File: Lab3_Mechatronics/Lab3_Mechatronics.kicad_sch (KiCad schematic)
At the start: 19 parts, among them Q1 Q_Photo_NPN, Q2 NMOS

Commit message: DO NOT USE 220 SHUNT 1K
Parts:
- added C1: 0.1u, symbol Device:C
- R3: value 220 -> 10k
- R7: value 1k -> 47k
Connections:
- net GND: now also C1.2
- net at D1.1 (K), L1.1, V3.1: now also C1.1
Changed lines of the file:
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@@
   (junction (at 66.04 113.03) (diameter 0) (color 0 0 0 0)
+  )
+  (junction (at 36.83 90.17) (diameter 0) (color 0 0 0 0)
+  )
+  (junction (at 36.83 111.76) (diameter 0) (color 0 0 0 0)
   )
   (junction (at 114.3 110.49) (diameter 0) (color 0 0 0 0)
@@
     (stroke (width 0) (type default))
   )
+  (wire (pts (xy 21.59 111.76) (xy 36.83 111.76))
+    (stroke (width 0) (type default))
+  )
   (wire (pts (xy 114.3 110.49) (xy 114.3 119.38))
     (stroke (width 0) (type default))
@@
     (stroke (width 0) (type default))
   )
+  (wire (pts (xy 21.59 90.17) (xy 36.83 90.17))
+    (stroke (width 0) (type default))
+  )
   (wire (pts (xy 54.61 128.27) (xy 54.61 138.43))
     (stroke (width 0) (type default))
   )
   (wire (pts (xy 66.04 113.03) (xy 66.04 115.57))
+    (stroke (width 0) (type default))
+  )
+  (wire (pts (xy 21.59 90.17) (xy 21.59 100.33))
     (stroke (width 0) (type default))
   )
@@
   )
   (wire (pts (xy 35.56 120.65) (xy 43.18 120.65))
+    (stroke (width 0) (type default))
+  )
+  (wire (pts (xy 21.59 107.95) (xy 21.59 111.76))
     (stroke (width 0) (type default))
   )
@@
       (effects (font (size 1.27 1.27)) (justify right))
     )
-    (property "Value" "1k" (at 57.15 125.73 0)
+    (property "Value" "47k" (at 57.15 125.73 0)
       (effects (font (size 1.27 1.27)) (justify right))
     )
@@
       (effects (font (size 1.27 1.27)))
     )
-    (property "Value" "220" (at 46.99 116.84 90)
+    (property "Value" "10k" (at 46.99 116.84 90)
       (effects (font (size 1.27 1.27)))
     )
@@
         )
       )
+    )
+  )
+  (symbol (lib_id "Device:C") (at 21.59 104.14 0) (unit 1)
+    (in_bom yes) (on_board yes) (dnp no) (fields_autoplaced)
+    (property "Reference" "C1" (at 25.4 102.87 0)
+      (effects (font (size 1.27 1.27)) (justify left))
+    )
+    (property "Value" "0.1u" (at 25.4 105.41 0)
+      (effects (font (size 1.27 1.27)) (justify left))
+    )
+    (property "Footprint" "" (at 22.5552 107.95 0)
+      (effects (font (size 1.27 1.27)) hide)
+    )
+    (property "Datasheet" "~" (at 21.59 104.14 0)
+      (effects (font (size 1.27 1.27)) hide)
+    )
+    (pin "1")
+    (pin "2")
+    (instances
+      (project "Lab3_Mechatronics"
+        (path "/33824bd4-7a24-4c2c-90db-ac51522648a8"
+          (reference "C1") (unit 1)
+        )
+      )

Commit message: replaced 220 with 470 ohm resistor
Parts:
- R1: value 220 -> 470
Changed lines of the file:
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@@
       (effects (font (size 1.27 1.27)) (justify left))
     )
-    (property "Value" "220" (at 46.99 43.18 0)
+    (property "Value" "470" (at 46.99 43.18 0)
       (effects (font (size 1.27 1.27)) (justify left))
     )

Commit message: replaced collector resistor with 47kohm
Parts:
- R2: value 4.7k -> 47k
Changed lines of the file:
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@@
       (effects (font (size 1.27 1.27)) (justify left))
     )
-    (property "Value" "4.7k" (at 90.17 43.18 0)
+    (property "Value" "47k" (at 90.17 43.18 0)
       (effects (font (size 1.27 1.27)) (justify left))
     )

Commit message: changed voltage source, and comment on back emf
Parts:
- V3: value 9 -> 10
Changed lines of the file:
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@@
     (fill (type none))
   )
-  (text_box "Note: Your backemf voltage here will not be negative, instead it will appear as being above the 12V voltage source"
+  (text_box "Note: Your backemf voltage on the oscilloscope will not be negative, instead it will appear as a voltage above the 10V voltage source."
     (at 72.39 82.55 0) (size 36.83 10.16)
     (stroke (width 0) (type default))
@@
       (effects (font (size 1.27 1.27) (color 0 0 1 1)) (justify left))
     )
-    (property "Value" "9" (at 31.75 104.14 0)
+    (property "Value" "10" (at 31.75 104.14 0)
       (effects (font (size 1.27 1.27) (color 0 0 1 1)) (justify left))
     )

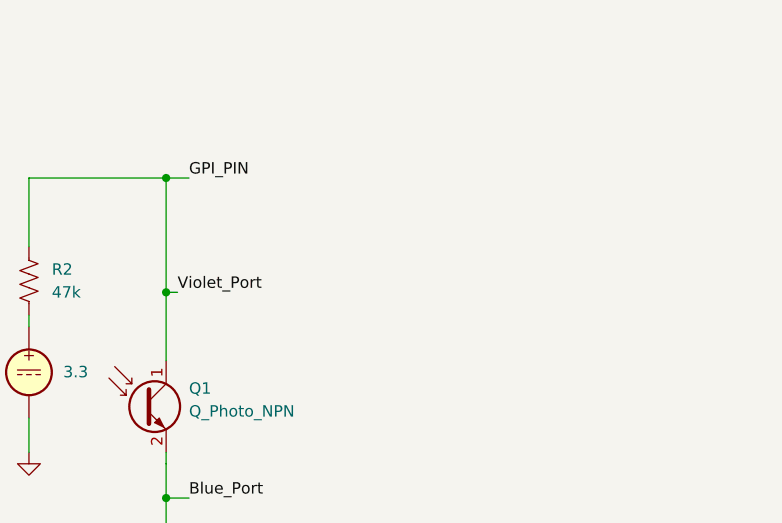
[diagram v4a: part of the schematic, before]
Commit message: added schmitt trigger to this circuit
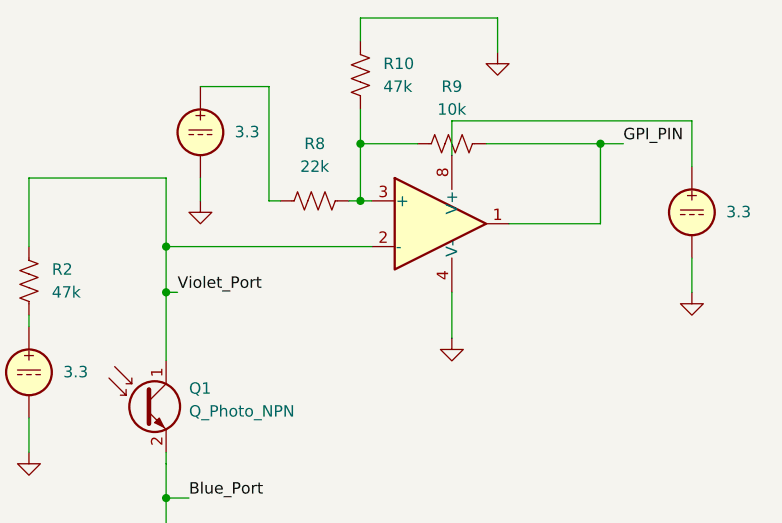
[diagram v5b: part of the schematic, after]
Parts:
- added R10: 47k, symbol Device:R_US
- added R8: 22k, symbol Device:R_US
- added R9: 10k, symbol Device:R_US
- added U1: LM358, symbol Amplifier_Operational:LM358
- added V5, V6: 3.3, symbol Simulation_SPICE:VDC
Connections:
- net GND: now also R10.2, U1.4 (V-), V5.2, V6.2
- net GPI_PIN: now also R9.2, U1.1; no longer Q1.1 (C), R2.1
- new net: U1.8 (V+), V5.1
- new net: R10.1, R8.2, R9.1, U1.3 (+)
- new net: R8.1, V6.1
- new net Violet_Port: Q1.1 (C), R2.1, U1.2 (-)

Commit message: unfinished lab 4 schem(in progress)
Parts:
- added C2: 0.1u, symbol Device:C
- R10: value 47k -> 22k
- R9: value 10k -> 47k
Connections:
- net GND: now also R9.2, C2.2; no longer R10.2
- net GPI_PIN: now also R10.2; no longer R9.2
- net Violet_Port: now also C2.1

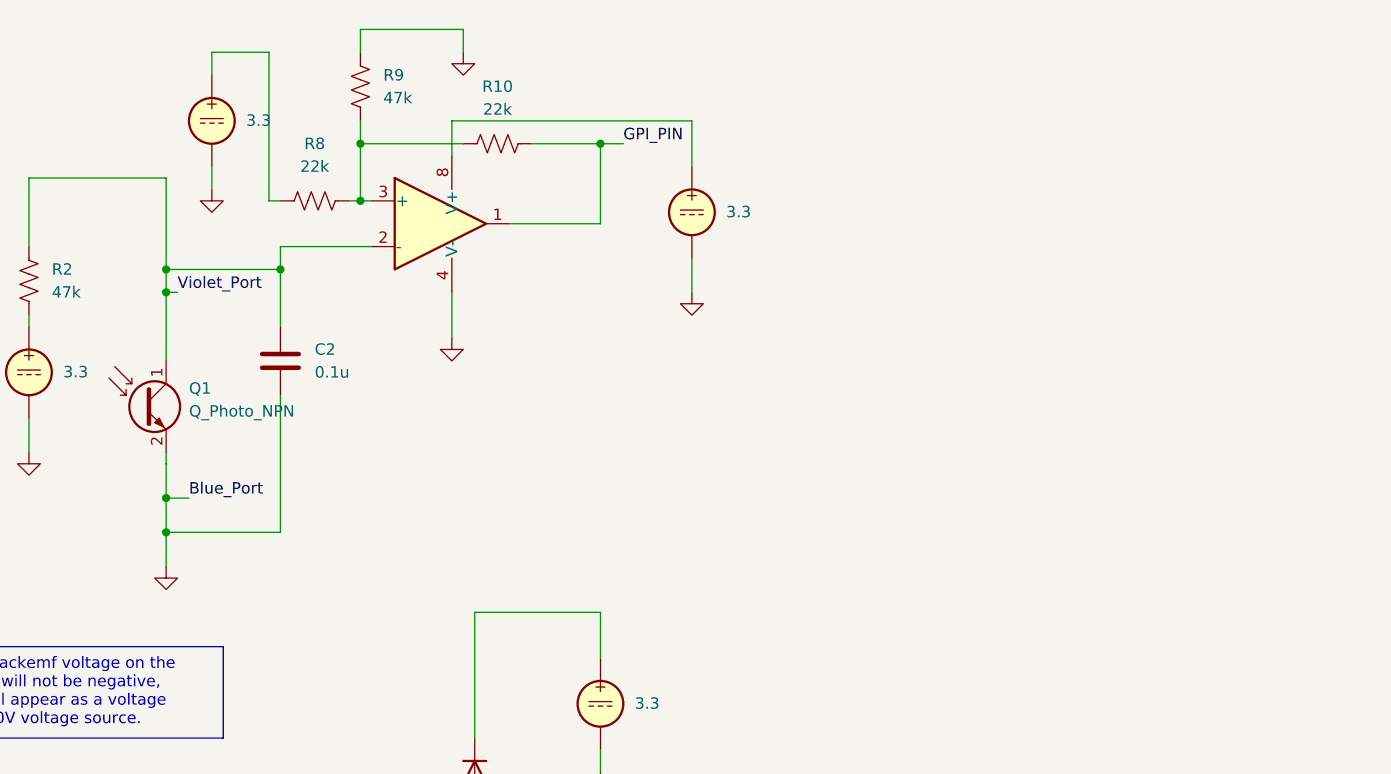
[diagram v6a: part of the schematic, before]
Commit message: updated lab 3 to explain schmitt trigger circuit
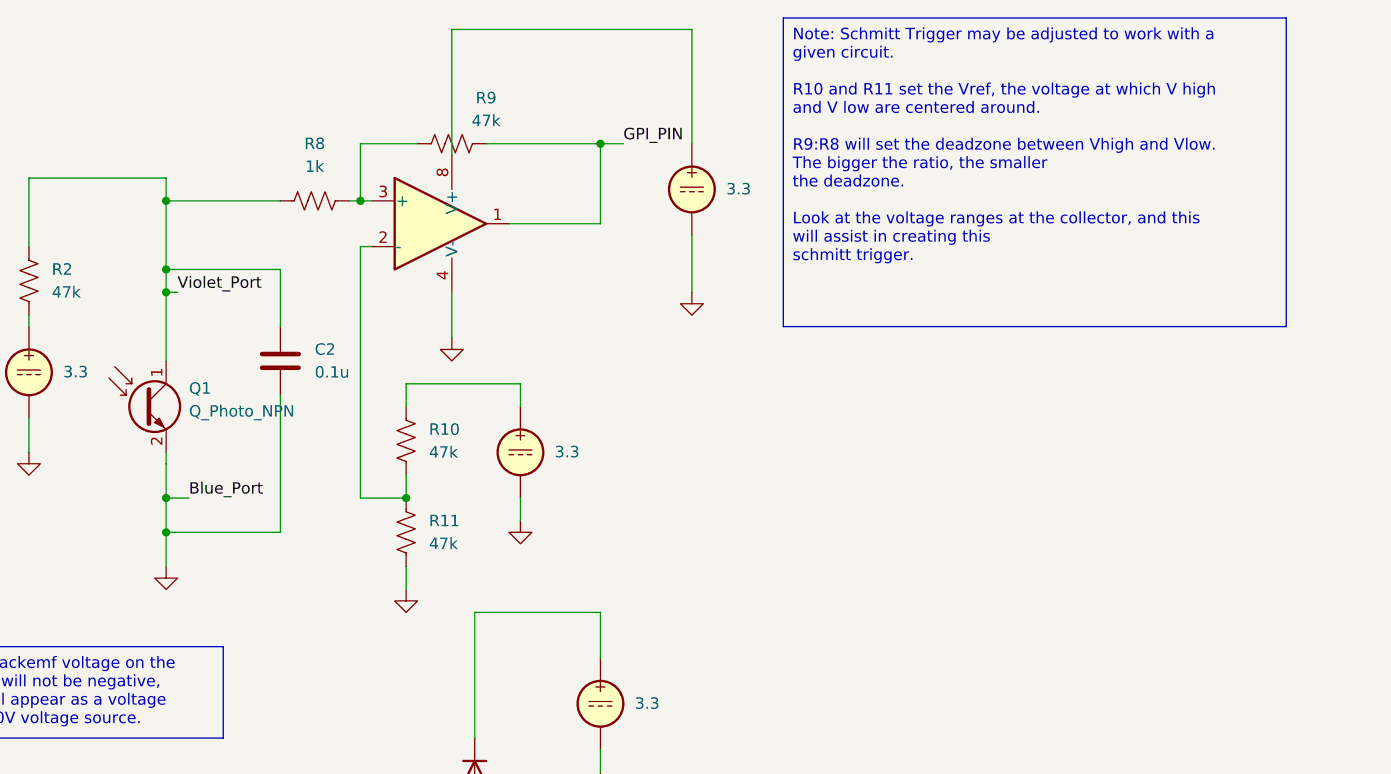
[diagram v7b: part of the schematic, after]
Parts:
- added R11: 47k, symbol Device:R_US
- R10: value 22k -> 47k
- R8: value 22k -> 1k
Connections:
- net GND: now also R11.2; no longer R9.2
- net GPI_PIN: now also R9.2; no longer R10.2
- net Violet_Port: now also R8.1; no longer U1.2 (-)
- net at R8.2, R9.1, U1.3 (+): no longer R10.1
- net at V6.1: now also R10.1; no longer R8.1
- new net: R10.2, R11.1, U1.2 (-)
